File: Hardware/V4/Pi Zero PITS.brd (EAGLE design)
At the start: 100.2 x 29.9 mm, 50 parts, among them IC1 MCP3426_ignore pin names, U1 U1, U2 LORA, U3 DS18B20, U4 MAX40200AUK+21-0057F_MXM-M, U5 MAX40200AUK+21-0057F_MXM-M

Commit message: Printed
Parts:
- removed U3: DS18B20, SparkFun-Sensors:TO-92-AMMO
- added U6: DS18B20, DS18B20:TO-92-TO92127P495H2044-3
- moved R1 3.71 mm to (24.5, 13.5)
- moved S+ 0.23 mm to (43.8, 11.0)
- moved S- 0.19 mm to (43.7, 39.2)
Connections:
- removed net N$1: +.1, RB1.2, SW1.1, SW1.2
- removed net N$18: C11.1, RB1.1, RB2.2, SW1.3, SW1.4, U5.1, U5.3
- net 3V3#1: now also U6.3; no longer U3.3
- net 5V_IN: now also +.1, C11.1, RB1.1, RB1.2, RB2.2, SW1.2, SW1.3, U5.1, U5.3
- net DQ: now also U6.2; no longer U3.2
- net GND: now also SW1.1, SW1.4, U6.1; no longer U3.1
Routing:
- net 5V_IN: track 57.6 -> 95.3 mm
- net N$18: track 22.9 -> 0.00 mm
- net N$1: track 9.79 -> 0.00 mm
- net DQ: track 43.4 -> 48.3 mm
- net 3V3#1: track 53.0 -> 56.9 mm
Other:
- board text added: "+44 7867 825 847"
- board text added: "If Found Please Call Kevin Walton"
- board text added: "JLCJLCJLCJLC"
- board text added: "PI Zero PITS V4"

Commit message: Updates
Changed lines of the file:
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@@
 <layer number="2" name="Route2" color="1" fill="3" visible="no" active="yes"/>
 <layer number="15" name="Route15" color="4" fill="6" visible="no" active="yes"/>
-<layer number="16" name="Bottom" color="1" fill="1" visible="no" active="yes"/>
+<layer number="16" name="Bottom" color="1" fill="1" visible="yes" active="yes"/>
 <layer number="17" name="Pads" color="2" fill="1" visible="yes" active="yes"/>
 <layer number="18" name="Vias" color="2" fill="1" visible="yes" active="yes"/>
@@
  Kevin   Walton</text>
 <text x="12.7" y="25.2476" size="1.6764" layer="25" font="vector" ratio="16" rot="R270" align="top-center">+44 7867   825 847</text>
+<polygon width="0.1524" layer="41">
+<vertex x="41.91" y="12.065"/>
+<vertex x="41.91" y="10.16"/>
+<vertex x="46.355" y="10.16"/>
+<vertex x="46.355" y="12.065"/>
+</polygon>
 </plain>
 <attributes>
@@
 <via x="60.3" y="39" extent="1-16" drill="0.35"/>
 <via x="57.7" y="39" extent="1-16" drill="0.35"/>
-<via x="46.5" y="11" extent="1-16" drill="0.35"/>
 <via x="49.5" y="11" extent="1-16" drill="0.35"/>
 <via x="48" y="11" extent="1-16" drill="0.35"/>
-<via x="41" y="11" extent="1-16" drill="0.35"/>
 <via x="39.5" y="11" extent="1-16" drill="0.35"/>
 <via x="38" y="11" extent="1-16" drill="0.35"/>
@@
 <via x="25.08" y="19.0588" extent="1-16" drill="0.35"/>
 <via x="25.715" y="19.0588" extent="1-16" drill="0.35"/>
-<via x="42.27" y="11" extent="1-16" drill="0.35"/>
 <via x="104.5" y="18.3302" extent="1-16" drill="0.35"/>
 <via x="104.6524" y="17.3396" extent="1-16" drill="0.35"/>

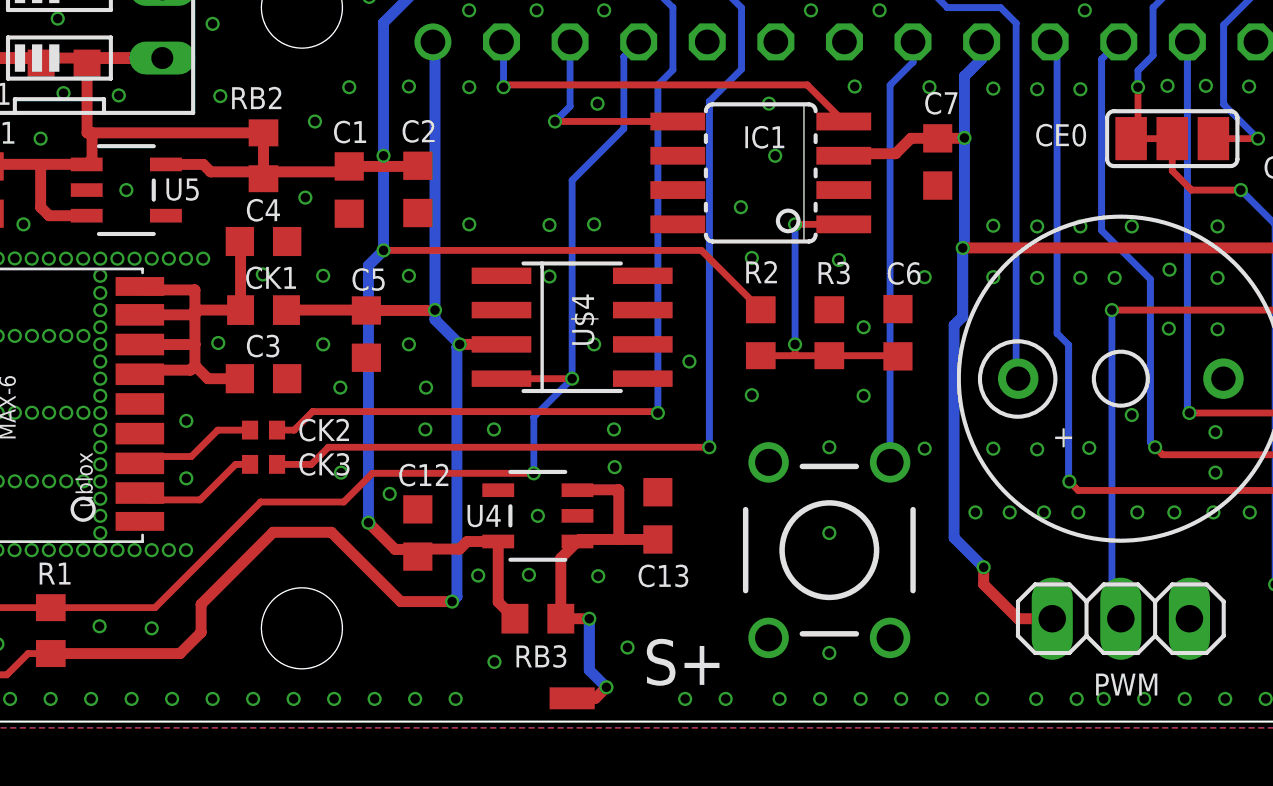
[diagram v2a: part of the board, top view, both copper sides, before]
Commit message: Added NMEA Logs, minor PCB updates, Git notes and Pi Ethernet Driver
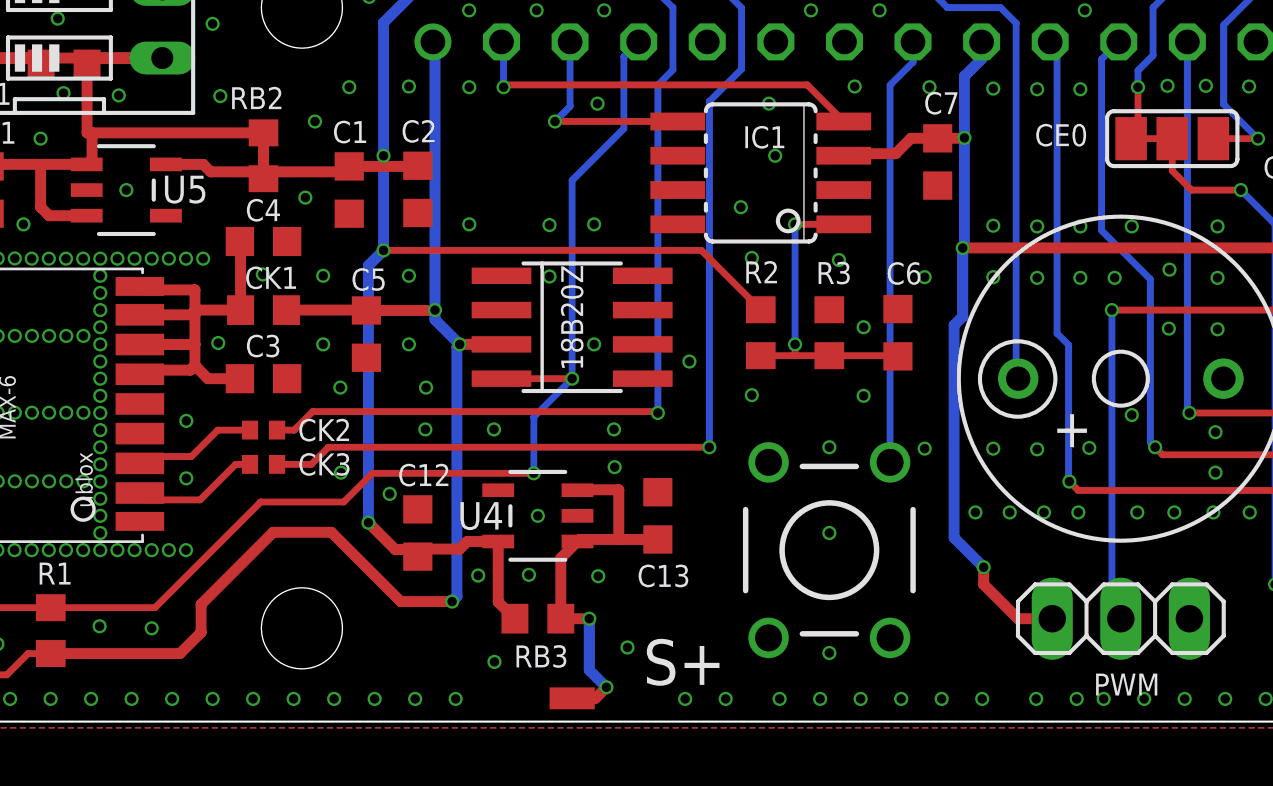
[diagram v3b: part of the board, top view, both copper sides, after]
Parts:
- renumbered U$4 to 18B20Z
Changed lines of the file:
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@@
 <hole x="98.4774" y="36.6014" drill="3"/>
 <hole x="98.4774" y="13.6144" drill="3"/>
-<text x="61.595" y="20.32" size="0.8128" layer="25" font="vector" ratio="19">+</text>
+<text x="61.595" y="20.32" size="1.4224" layer="25" font="vector" ratio="19">+</text>
 <text x="88.265" y="12.065" size="1.778" layer="26" rot="MR0">JLCJLCJLCJLC</text>
 <text x="9.8806" y="25.2476" size="1.0922" layer="25" font="vector" ratio="16" rot="R270" align="top-center">If Found Please Call
@@
 <attribute name="SPICEPREFIX" value="R" x="32.385" y="25.4" size="1.778" layer="27" rot="R180" display="off"/>
 </element>
-<element name="U$4" library="ava" package="DS18B20_SOIC" value="DS1820SOIC" x="43.815" y="24.765" smashed="yes" rot="R270">
-<attribute name="NAME" x="43.815" y="26.035" size="0.8128" layer="25" font="vector" ratio="19" rot="R270"/>
+<element name="18B20Z" library="ava" package="DS18B20_SOIC" value="DS1820SOIC" x="43.815" y="24.765" smashed="yes" rot="R270">
+<attribute name="NAME" x="43.4086" y="27.0764" size="0.8128" layer="25" font="vector" ratio="19" rot="R270"/>
 </element>
 <element name="CK2" library="rcl" library_urn="urn:adsk.eagle:library:334" package="R0402" package3d_urn="urn:adsk.eagle:package:23547/2" value="BLM15HD102SN1D" x="32.385" y="20.955" smashed="yes">
@@
 <attribute name="COPYRIGHT" value="Copyright (C) 2018 Accelerated Designs. All rights reserved" x="42.545" y="17.78" size="1.778" layer="27" rot="R180" display="off"/>
 <attribute name="MANUFACTURER_PART_NUMBER" value="MAX40200AUK+" x="42.545" y="17.78" size="1.778" layer="27" rot="R180" display="off"/>
-<attribute name="NAME" x="39.8526" y="17.3736" size="0.8128" layer="25" font="vector" ratio="19" rot="SR0"/>
+<attribute name="NAME" x="39.5732" y="17.272" size="1.016" layer="25" font="vector" ratio="19" rot="SR0"/>
 <attribute name="SOURCELIBRARY" value="Maxim_2018-11-30" x="42.545" y="17.78" size="1.778" layer="27" rot="R180" display="off"/>
 <attribute name="VENDOR" value="Maxim Integrated Products" x="42.545" y="17.78" size="1.778" layer="27" rot="R180" display="off"/>
@@
 </element>
 <element name="S+" library="KEW_HF_V13" package="SMD_SMALL" value="" x="43.815" y="11.0236" smashed="yes" rot="R90">
-<attribute name="NAME" x="49.4916" y="13.1954" size="1.6764" layer="25" font="vector" ratio="15" rot="R180"/>
+<attribute name="NAME" x="49.4916" y="13.1954" size="1.6764" layer="25" font="vector" ratio="19" rot="R180"/>
 <attribute name="VALUE" x="43.815" y="11.0236" size="0.0254" layer="27" rot="R90"/>
 </element>
@@
 <attribute name="COPYRIGHT" value="Copyright (C) 2018 Accelerated Designs. All rights reserved" x="27.305" y="29.845" size="1.778" layer="27" display="off"/>
 <attribute name="MANUFACTURER_PART_NUMBER" value="MAX40200AUK+" x="27.305" y="29.845" size="1.778" layer="27" display="off"/>
-<attribute name="NAME" x="28.702" y="29.464" size="0.8128" layer="25" font="vector" ratio="19" rot="SR0"/>
+<attribute name="NAME" x="28.6258" y="29.3624" size="1.016" layer="25" font="vector" ratio="20" rot="SR0"/>
 <attribute name="SOURCELIBRARY" value="Maxim_2018-11-30" x="27.305" y="29.845" size="1.778" layer="27" display="off"/>
 <attribute name="VENDOR" value="Maxim Integrated Products" x="27.305" y="29.845" size="1.778" layer="27" display="off"/>
@@
 <contactref element="C10" pad="2"/>
 <contactref element="C4" pad="2"/>
-<contactref element="U$4" pad="GND"/>
+<contactref element="18B20Z" pad="GND"/>
 <via x="55.2" y="39" extent="1-16" drill="0.35"/>
 <via x="52.7" y="39" extent="1-16" drill="0.35"/>
@@
 <contactref element="R1" pad="2"/>
 <contactref element="SV1" pad="7"/>
-<contactref element="U$4" pad="DQ"/>
+<contactref element="18B20Z" pad="DQ"/>
 <wire x1="43.815" y1="22.86" x2="41.1988" y2="22.86" width="0.254" layer="1"/>
 <via x="43.815" y="22.86" extent="1-16" drill="0.35"/>
@@
 <wire x1="36.181" y1="25.4" x2="33.235" y2="25.4" width="0.4064" layer="1"/>
 <contactref element="R1" pad="1"/>
-<contactref element="U$4" pad="VCC"/>
+<contactref element="18B20Z" pad="VCC"/>
 <wire x1="24.5072" y1="12.68" x2="23.669" y2="12.68" width="0.254" layer="1"/>
 <wire x1="23.669" y1="12.68" x2="22.8816" y2="11.8926" width="0.254" layer="1"/>

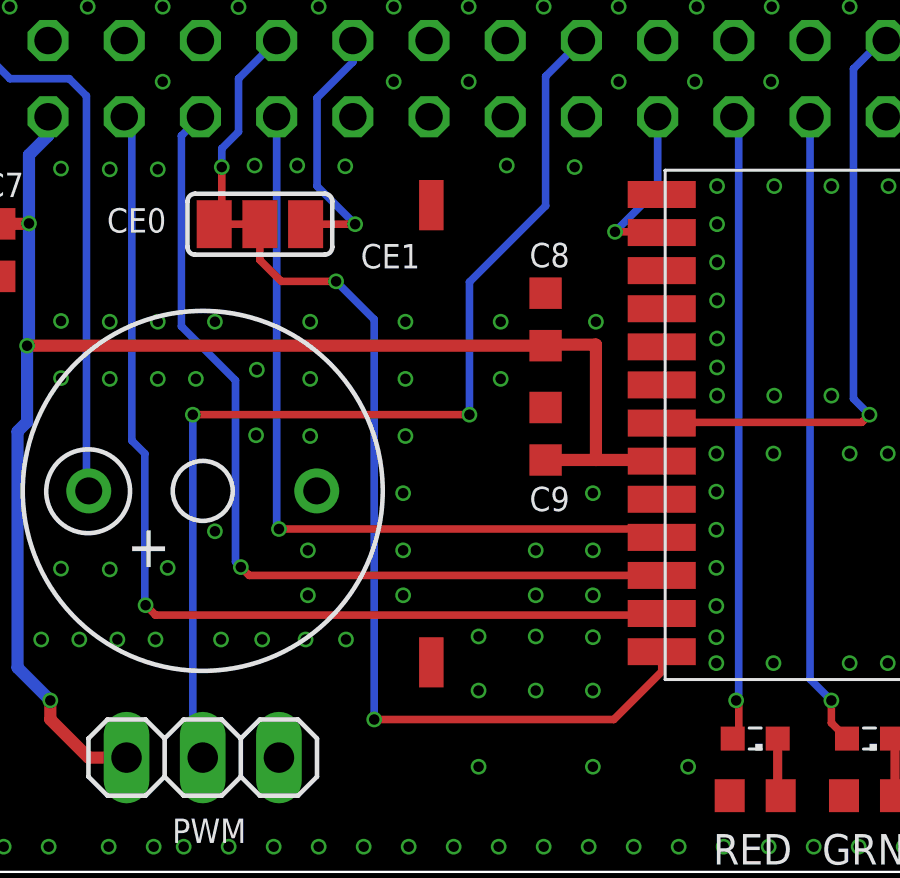
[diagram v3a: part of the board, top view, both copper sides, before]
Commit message: Moved Solar support pads to between GPIO pins
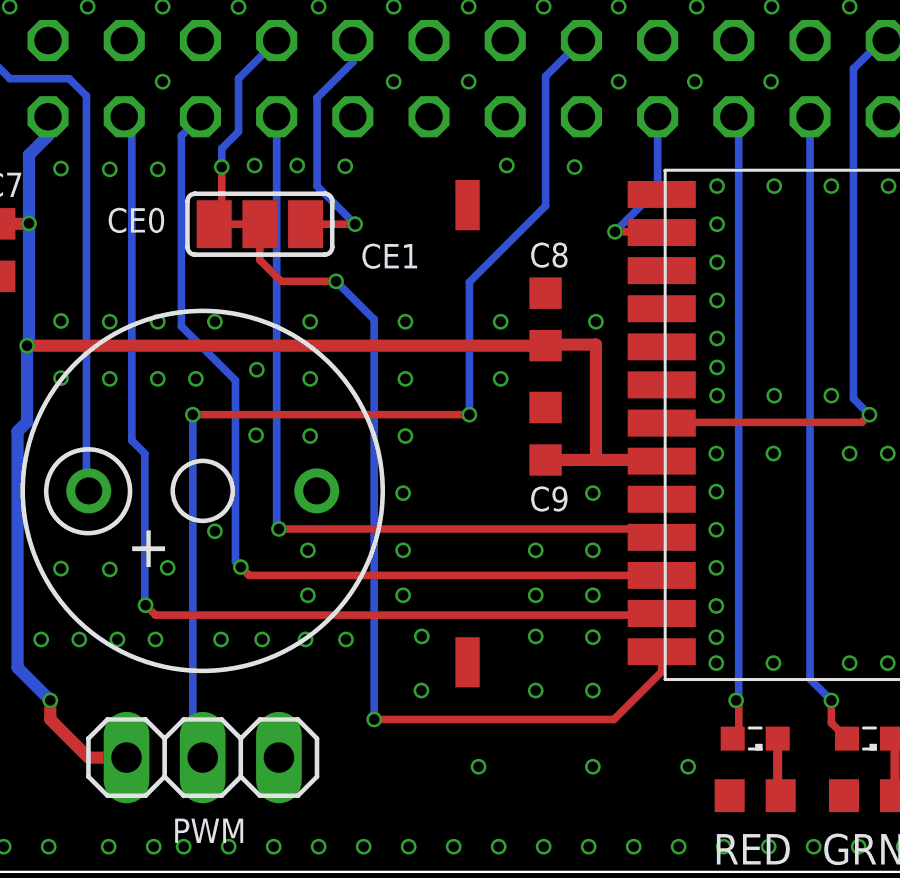
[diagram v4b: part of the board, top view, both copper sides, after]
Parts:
- moved PAD4 1.21 mm to (73.0, 32.4)
- moved PAD5 1.21 mm to (73.0, 17.1)
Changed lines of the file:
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@@
 <setting verticaltext="up"/>
 </settings>
-<grid distance="25" unitdist="mil" unit="mil" style="lines" multiple="1" display="yes" altdistance="1" altunitdist="mil" altunit="mil"/>
+<grid distance="25" unitdist="mil" unit="mil" style="lines" multiple="1" display="yes" altdistance="2.5" altunitdist="mil" altunit="mil"/>
 <layers>
 <layer number="1" name="Top" color="4" fill="1" visible="yes" active="yes"/>
@@
 <attribute name="VENDOR" value="Maxim Integrated Products" x="27.305" y="29.845" size="1.778" layer="27" display="off"/>
 </element>
-<element name="PAD4" library="KEW_HF_V13" package="SMD_SMALL" value="" x="71.755" y="32.385" smashed="yes">
-<attribute name="VALUE" x="71.755" y="32.385" size="0.0254" layer="27"/>
-</element>
-<element name="PAD5" library="KEW_HF_V13" package="SMD_SMALL" value="" x="71.755" y="17.145" smashed="yes">
-<attribute name="VALUE" x="71.755" y="17.145" size="0.0254" layer="27"/>
+<element name="PAD4" library="KEW_HF_V13" package="SMD_SMALL" value="" x="72.9615" y="32.385" smashed="yes">
+<attribute name="VALUE" x="72.9615" y="32.385" size="0.0254" layer="27"/>
+</element>
+<element name="PAD5" library="KEW_HF_V13" package="SMD_SMALL" value="" x="72.9615" y="17.145" smashed="yes">
+<attribute name="VALUE" x="72.9615" y="17.145" size="0.0254" layer="27"/>
 </element>
 <element name="C11" library="rcl" library_urn="urn:adsk.eagle:library:334" package="C0603K" package3d_urn="urn:adsk.eagle:package:23680/2" value="100nF 0603" x="22.225" y="29.845" smashed="yes" rot="R270">
@@
 <via x="77.1398" y="17.9832" extent="1-16" drill="0.35"/>
 <via x="77.1398" y="16.2052" extent="1-16" drill="0.35"/>
-<via x="73.3298" y="16.2052" extent="1-16" drill="0.35"/>
-<via x="73.3298" y="18.0086" extent="1-16" drill="0.35"/>
+<via x="71.4248" y="16.2052" extent="1-16" drill="0.35"/>
+<via x="71.4375" y="18.0086" extent="1-16" drill="0.35"/>
 <via x="73.3298" y="13.6652" extent="1-16" drill="0.35"/>
 <via x="77.1398" y="13.6652" extent="1-16" drill="0.35"/>

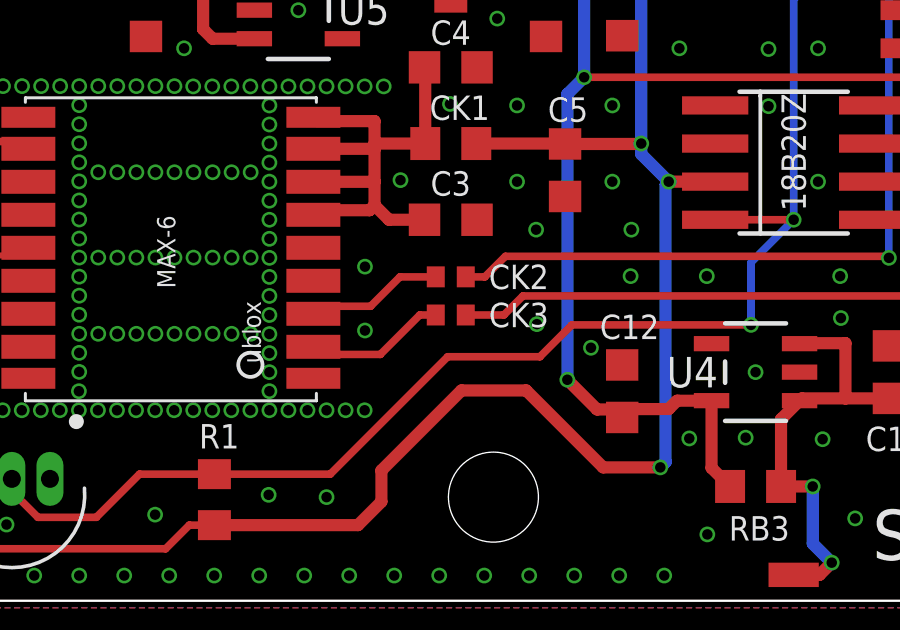
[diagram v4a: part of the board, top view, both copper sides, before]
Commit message: Restrict ground plane next to cut-able tracks
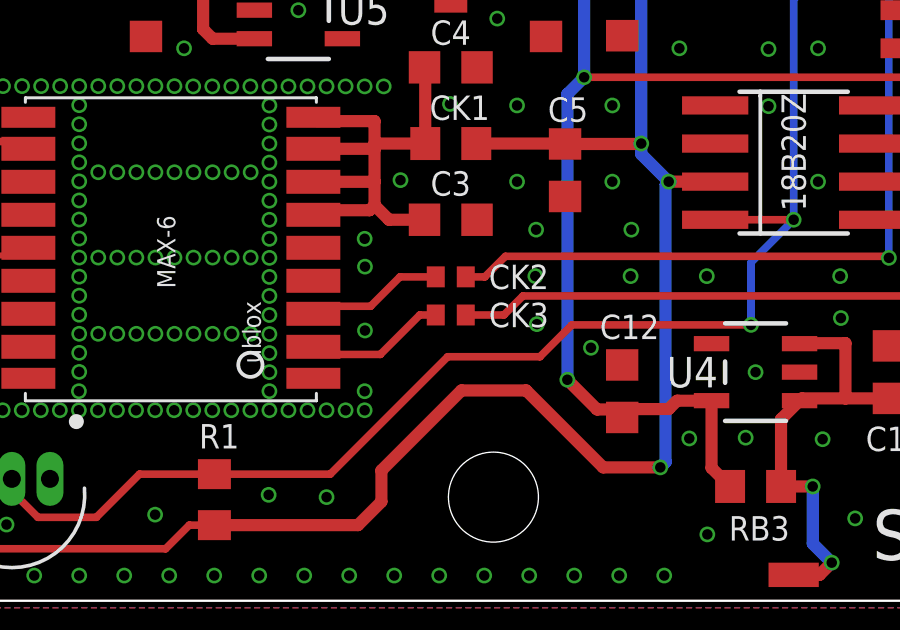
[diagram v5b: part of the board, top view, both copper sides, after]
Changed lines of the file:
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@@
 <vertex x="46.355" y="12.065"/>
+</polygon>
+<polygon width="0.1524" layer="41">
+<vertex x="23.622" y="35.1155"/>
+<vertex x="26.416" y="35.1155"/>
+<vertex x="26.416" y="33.909"/>
+<vertex x="23.5585" y="33.909"/>
+<vertex x="23.5585" y="35.052"/>
+</polygon>
+<polygon width="0.1524" layer="41">
+<vertex x="31.75" y="32.512"/>
+<vertex x="31.75" y="29.718"/>
+<vertex x="33.02" y="29.718"/>
+<vertex x="33.02" y="32.512"/>
 </polygon>
 </plain>
@@
 <via x="95.635" y="35.19" extent="1-16" drill="0.35"/>
 <via x="95.5294" y="13.6906" extent="1-16" drill="0.35"/>
+<via x="35.2044" y="20.9804" extent="1-16" drill="0.35"/>
+<via x="29.5148" y="17.145" extent="1-16" drill="0.35"/>
+<via x="29.5148" y="22.225" extent="1-16" drill="0.35"/>
 <wire x1="102.8624" y1="22.3012" x2="101.5" y2="22.125" width="0" layer="19" extent="16-16"/>
 </signal>
